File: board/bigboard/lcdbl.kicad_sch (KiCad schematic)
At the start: 5 parts, among them J10 Conn_02x03_Row_Letter_First, J9 Conn_01x05_Male

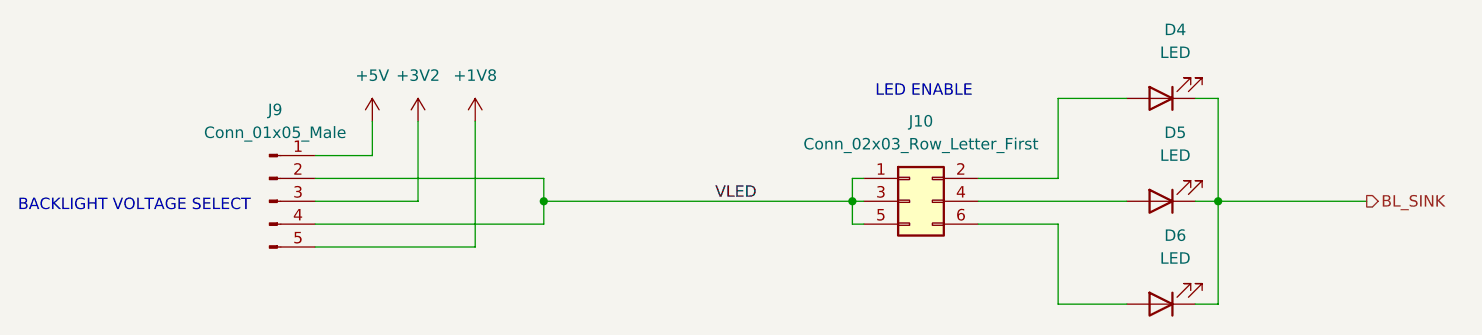
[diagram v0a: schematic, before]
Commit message: Manufactured version of bigboard
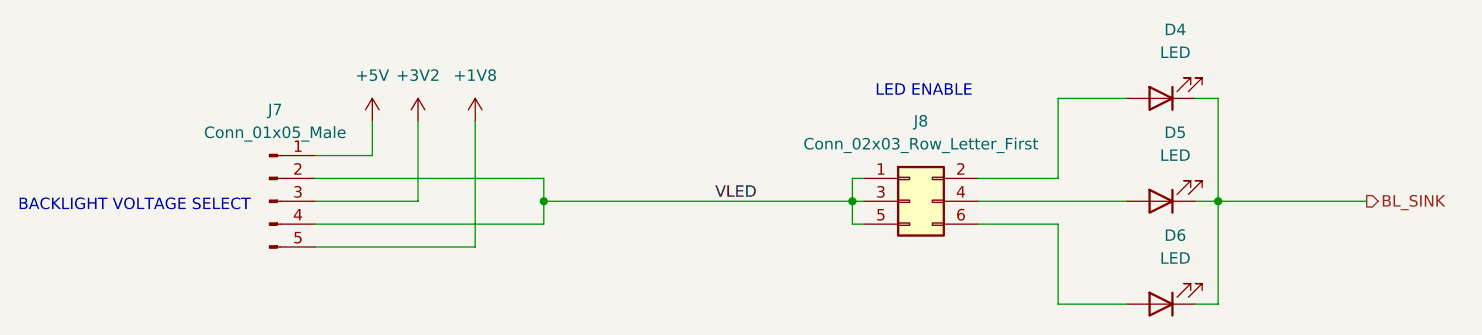
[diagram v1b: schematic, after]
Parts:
- renumbered J9 to J7, J10 to J8
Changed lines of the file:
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@@
   (symbol (lib_id "power:+5V") (at 107.95 95.25 0) (unit 1)
     (in_bom yes) (on_board yes) (fields_autoplaced)
-    (property "Reference" "#PWR034" (id 0) (at 107.95 99.06 0)
+    (property "Reference" "#PWR030" (id 0) (at 107.95 99.06 0)
       (effects (font (size 1.27 1.27)) hide)
     )
@@
   (symbol (lib_id "power:+1V8") (at 119.38 95.25 0) (unit 1)
     (in_bom yes) (on_board yes) (fields_autoplaced)
-    (property "Reference" "#PWR036" (id 0) (at 119.38 99.06 0)
+    (property "Reference" "#PWR032" (id 0) (at 119.38 99.06 0)
       (effects (font (size 1.27 1.27)) hide)
     )
@@
   (symbol (lib_id "Connector:Conn_01x05_Male") (at 96.52 104.14 0) (unit 1)
     (in_bom yes) (on_board yes) (fields_autoplaced)
-    (property "Reference" "J9" (id 0) (at 97.155 93.98 0))
+    (property "Reference" "J7" (id 0) (at 97.155 93.98 0))
     (property "Value" "Conn_01x05_Male" (id 1) (at 97.155 96.52 0))
     (property "Footprint" "Connector_PinHeader_2.54mm:PinHeader_1x05_P2.54mm_Vertical" (id 2) (at 96.52 104.14 0)
@@
   (symbol (lib_id "Connector_Generic:Conn_02x03_Odd_Even") (at 167.64 104.14 0) (unit 1)
     (in_bom yes) (on_board yes) (fields_autoplaced)
-    (property "Reference" "J10" (id 0) (at 168.91 95.25 0))
+    (property "Reference" "J8" (id 0) (at 168.91 95.25 0))
     (property "Value" "Conn_02x03_Row_Letter_First" (id 1) (at 168.91 97.79 0))
     (property "Footprint" "Connector_PinHeader_2.54mm:PinHeader_2x03_P2.54mm_Vertical" (id 2) (at 167.64 104.14 0)
@@
   (symbol (lib_id "3v2:+3V2") (at 113.03 95.25 0) (unit 1)
     (in_bom yes) (on_board yes) (fields_autoplaced)
-    (property "Reference" "#PWR035" (id 0) (at 113.03 99.06 0)
+    (property "Reference" "#PWR031" (id 0) (at 113.03 99.06 0)
       (effects (font (size 1.27 1.27)) hide)
     )
